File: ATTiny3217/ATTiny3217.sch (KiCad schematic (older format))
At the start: 22 parts, among them J1 Conn_01x12, J2 Conn_01x02, J3 Conn_01x12, J4 ISP6, SW1 RST, U1 AP2204K-ADJ, U2 ATtiny3217-M

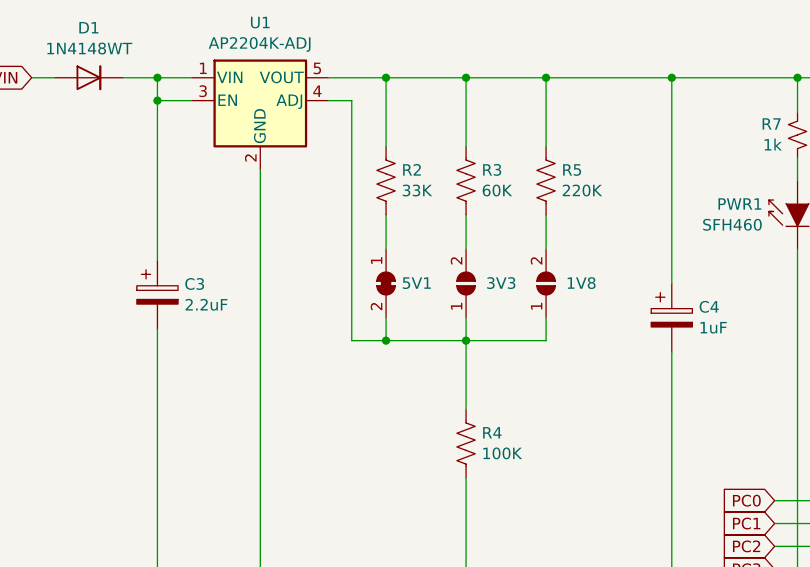
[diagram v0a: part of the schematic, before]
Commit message: Silkscreens Orientated
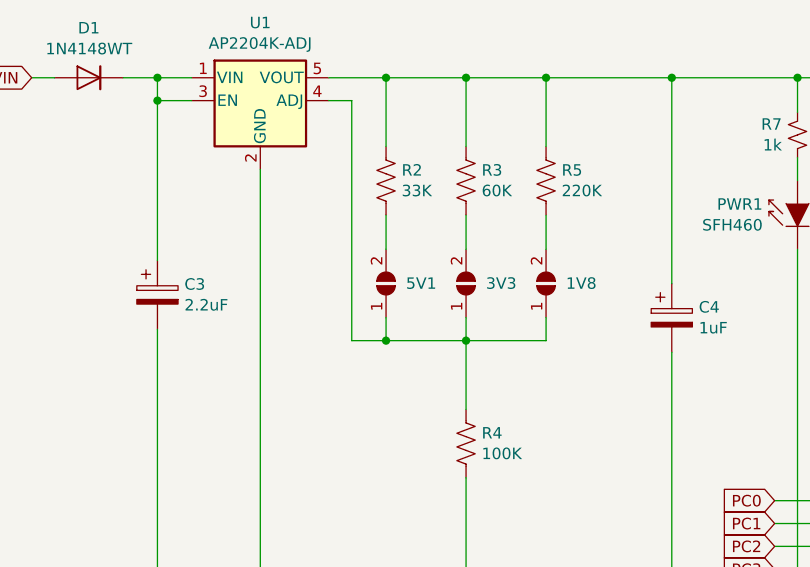
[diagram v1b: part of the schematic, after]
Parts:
- removed 5V1: SolderJumper_2_Bridged, Jumper:SolderJumper-2_P1.3mm_Bridged_RoundedPad1.0x1.5mm, symbol Jumper:SolderJumper_2_Bridged
- added 5V1: SolderJumper_2_Open, Jumper:SolderJumper-2_P1.3mm_Open_RoundedPad1.0x1.5mm, symbol Jumper:SolderJumper_2_Open
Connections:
- net at R2.2: now also 5V1.2 (B)
- net at 1V8.1 (A), 3V3.1 (A), R4.1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: now also 5V1.1 (A)
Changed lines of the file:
@@
 Wire Wire Line
 	3900 2400 4000 2400
-$Comp
-L Jumper:SolderJumper_2_Bridged 5V1
-U 1 1 5D4D08FE
-P 4150 3200
-F 0 "5V1" V 4150 3268 50  0000 L CNN
-F 1 "SolderJumper_2_Bridged" V 4195 3268 50  0001 L CNN
-F 2 "Jumper:SolderJumper-2_P1.3mm_Bridged_RoundedPad1.0x1.5mm" H 4150 3200 50  0001 C CNN
-F 3 "~" H 4150 3200 50  0001 C CNN
-	1    4150 3200
-	0    1    1    0
-$EndComp
 Wire Wire Line
 	4850 2900 4850 3050
@@
 Wire Wire Line
 	10500 4150 10600 4150
+$Comp
+L Jumper:SolderJumper_2_Open 5V1
+U 1 1 5D5F26DA
+P 4150 3200
+F 0 "5V1" V 4150 3113 50  0000 R CNN
+F 1 "SolderJumper_2_Open" H 4150 3313 50  0001 C CNN
+F 2 "Jumper:SolderJumper-2_P1.3mm_Open_RoundedPad1.0x1.5mm" H 4150 3200 50  0001 C CNN
+F 3 "~" H 4150 3200 50  0001 C CNN
+	1    4150 3200
+	0    -1   -1   0
+$EndComp
 $EndSCHEMATC
